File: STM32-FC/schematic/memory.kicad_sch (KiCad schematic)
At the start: 9 parts, among them J4 DM3AT-SF-PEJM5, U10 W25Q32JVUUIQ

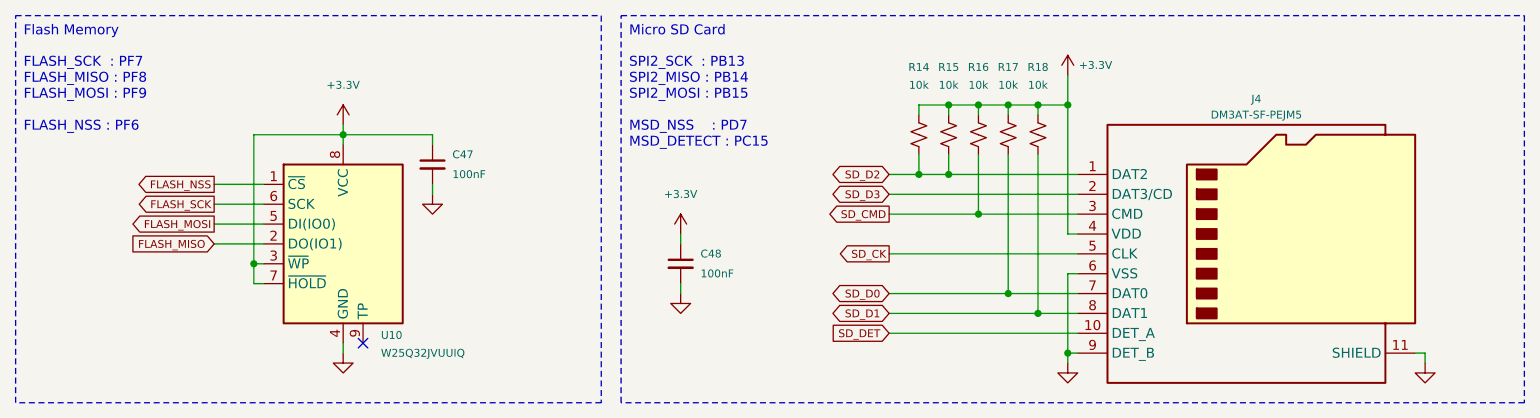
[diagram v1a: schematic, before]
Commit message: update : BOM and minor fix
- remove : DC2DC for analog
- change : JST SM conn. to BM
- change : ELRS conn. to JST XH (instead of JST SM)
- update : BOM List
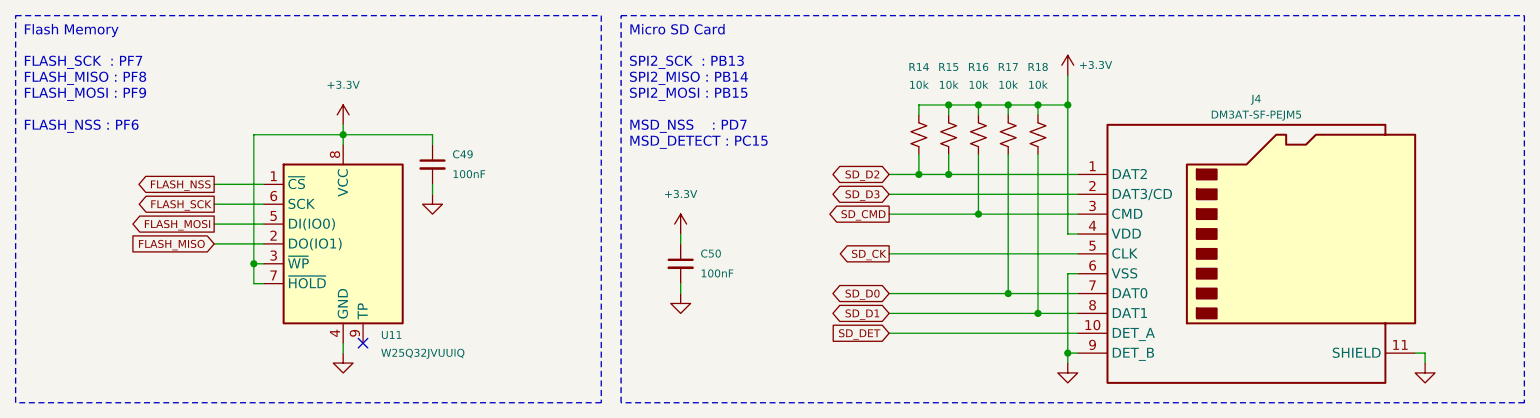
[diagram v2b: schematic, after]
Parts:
- renumbered C47 to C49, C48 to C50, U10 to U11
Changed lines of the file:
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@@
 		(dnp no)
 		(fields_autoplaced yes)
-		(property "Reference" "#PWR084"
+		(property "Reference" "#PWR089"
 			(at 107.95 54.61 0)
 			(effects
@@
 			(project ""
 				(path "/8d4cc317-3933-4aa6-844b-8c5c635e89c7/3e7c6c79-bc31-4cc9-af6a-d0a28245a7b2"
-					(reference "#PWR084")
+					(reference "#PWR089")
 					(unit 1)
 				)
@@
 		(dnp no)
 		(fields_autoplaced yes)
-		(property "Reference" "#PWR082"
+		(property "Reference" "#PWR087"
 			(at 76.2 41.91 0)
 			(effects
@@
 			(project ""
 				(path "/8d4cc317-3933-4aa6-844b-8c5c635e89c7/3e7c6c79-bc31-4cc9-af6a-d0a28245a7b2"
-					(reference "#PWR082")
+					(reference "#PWR087")
 					(unit 1)
 				)
@@
 		(dnp no)
 		(fields_autoplaced yes)
-		(property "Reference" "#PWR080"
+		(property "Reference" "#PWR085"
 			(at 64.77 30.48 0)
 			(effects
@@
 			(project ""
 				(path "/8d4cc317-3933-4aa6-844b-8c5c635e89c7/3e7c6c79-bc31-4cc9-af6a-d0a28245a7b2"
-					(reference "#PWR080")
+					(reference "#PWR085")
 					(unit 1)
 				)
@@
 		(dnp no)
 		(fields_autoplaced yes)
-		(property "Reference" "#PWR086"
+		(property "Reference" "#PWR091"
 			(at 157.48 63.5 0)
 			(effects
@@
 			(project "STM32-FC"
 				(path "/8d4cc317-3933-4aa6-844b-8c5c635e89c7/3e7c6c79-bc31-4cc9-af6a-d0a28245a7b2"
-					(reference "#PWR086")
+					(reference "#PWR091")
 					(unit 1)
 				)
@@
 		(on_board yes)
 		(dnp no)
-		(property "Reference" "C47"
+		(property "Reference" "C49"
 			(at 78.74 30.48 0)
 			(effects
@@
 			(project "STM32-FC"
 				(path "/8d4cc317-3933-4aa6-844b-8c5c635e89c7/3e7c6c79-bc31-4cc9-af6a-d0a28245a7b2"
-					(reference "C47")
+					(reference "C49")
 					(unit 1)
 				)
@@
 		(on_board yes)
 		(dnp no)
-		(property "Reference" "C48"
+		(property "Reference" "C50"
 			(at 110.49 43.18 0)
 			(effects
@@
 			(project "STM32-FC"
 				(path "/8d4cc317-3933-4aa6-844b-8c5c635e89c7/3e7c6c79-bc31-4cc9-af6a-d0a28245a7b2"
-					(reference "C48")
+					(reference "C50")
 					(unit 1)
 				)
@@
 		(dnp no)
 		(fields_autoplaced yes)
-		(property "Reference" "#PWR083"
+		(property "Reference" "#PWR088"
 			(at 107.95 44.45 0)
 			(effects
@@
 			(project ""
 				(path "/8d4cc317-3933-4aa6-844b-8c5c635e89c7/3e7c6c79-bc31-4cc9-af6a-d0a28245a7b2"
-					(reference "#PWR083")
+					(reference "#PWR088")
 					(unit 1)
 				)
@@
 		(dnp no)
 		(fields_autoplaced yes)
-		(property "Reference" "#PWR087"
+		(property "Reference" "#PWR092"
 			(at 203.2 63.5 0)
 			(effects
@@
 			(project "STM32-FC"
 				(path "/8d4cc317-3933-4aa6-844b-8c5c635e89c7/3e7c6c79-bc31-4cc9-af6a-d0a28245a7b2"
-					(reference "#PWR087")
+					(reference "#PWR092")
 					(unit 1)
 				)
@@
 		(dnp no)
 		(fields_autoplaced yes)
-		(property "Reference" "#PWR081"
+		(property "Reference" "#PWR086"
 			(at 64.77 62.23 0)
 			(effects
@@
 			(project ""
 				(path "/8d4cc317-3933-4aa6-844b-8c5c635e89c7/3e7c6c79-bc31-4cc9-af6a-d0a28245a7b2"
-					(reference "#PWR081")
+					(reference "#PWR086")
 					(unit 1)
 				)
@@
 		(on_board yes)
 		(dnp no)
-		(property "Reference" "U10"
+		(property "Reference" "U11"
 			(at 69.596 53.594 0)
 			(effects
@@
 			(project "STM32-FC"
 				(path "/8d4cc317-3933-4aa6-844b-8c5c635e89c7/3e7c6c79-bc31-4cc9-af6a-d0a28245a7b2"
-					(reference "U10")
+					(reference "U11")
 					(unit 1)
 				)
@@
 		(on_board yes)
 		(dnp no)
-		(property "Reference" "#PWR085"
+		(property "Reference" "#PWR090"
 			(at 157.48 24.13 0)
 			(effects
@@
 			(project "STM32-FC"
 				(path "/8d4cc317-3933-4aa6-844b-8c5c635e89c7/3e7c6c79-bc31-4cc9-af6a-d0a28245a7b2"
-					(reference "#PWR085")
+					(reference "#PWR090")
 					(unit 1)
 				)

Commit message: change : RC size 0402 to 0201
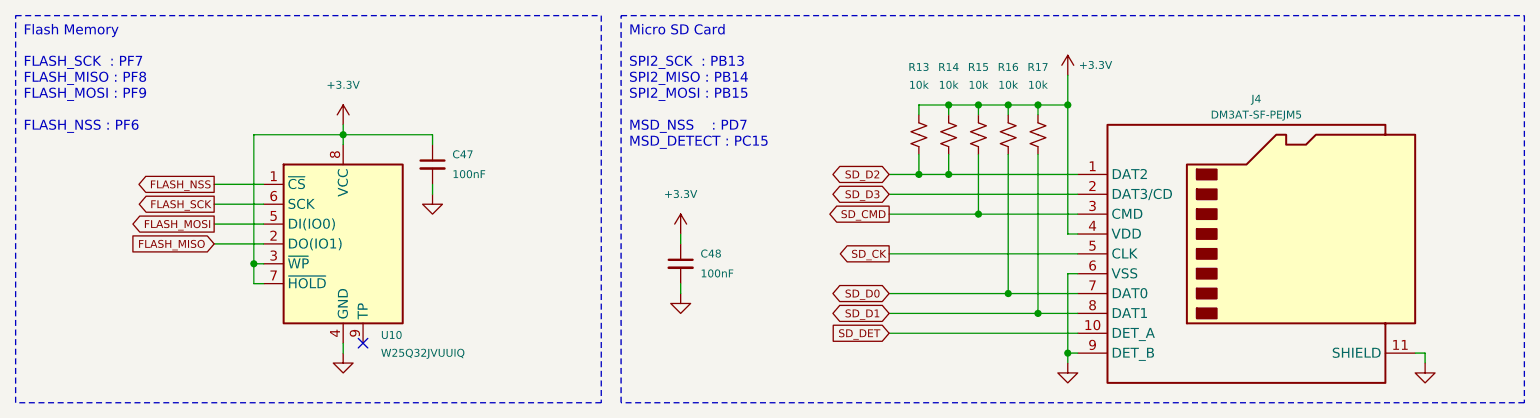
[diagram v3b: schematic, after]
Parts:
- C47: renamed from C49; footprint Capacitor_SMD:C_0402_1005Metric -> Capacitor_SMD:C_0201_0603Metric; LCSC C1525 -> C49062
- C48: renamed from C50; footprint Capacitor_SMD:C_0402_1005Metric -> Capacitor_SMD:C_0201_0603Metric; LCSC C1525 -> C49062
- R13: renamed from R14; footprint Resistor_SMD:R_0402_1005Metric -> Resistor_SMD:R_0201_0603Metric; LCSC C25531 -> C106225
- R14: renamed from R15; footprint Resistor_SMD:R_0402_1005Metric -> Resistor_SMD:R_0201_0603Metric; LCSC C25531 -> C106225
- R15: renamed from R16; footprint Resistor_SMD:R_0402_1005Metric -> Resistor_SMD:R_0201_0603Metric; LCSC C25531 -> C106225
- R16: renamed from R17; footprint Resistor_SMD:R_0402_1005Metric -> Resistor_SMD:R_0201_0603Metric; LCSC C25531 -> C106225
- R17: renamed from R18; footprint Resistor_SMD:R_0402_1005Metric -> Resistor_SMD:R_0201_0603Metric; LCSC C25531 -> C106225
- renumbered U11 to U10
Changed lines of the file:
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@@
 		(on_board yes)
 		(dnp no)
-		(property "Reference" "R18"
+		(property "Reference" "R17"
 			(at 153.67 19.304 0)
 			(effects
@@
 			)
 		)
-		(property "Footprint" "Resistor_SMD:R_0402_1005Metric"
+		(property "Footprint" "Resistor_SMD:R_0201_0603Metric"
 			(at 153.67 27.94 0)
 			(effects
@@
 			)
 		)
-		(property "Description" "Resistor, small US symbol"
+		(property "Description" "-55℃~+125℃ 10kΩ 25V 50mW Thick Film Resistor ±1% ±200ppm/℃ 0201 Chip Resistor - Surface Mount ROHS"
 			(at 153.67 27.94 0)
 			(effects
@@
 			)
 		)
-		(property "LCSC" "C25531"
+		(property "LCSC" "C106225"
 			(at 153.67 27.94 0)
 			(effects
@@
 			(project "STM32-FC"
 				(path "/8d4cc317-3933-4aa6-844b-8c5c635e89c7/3e7c6c79-bc31-4cc9-af6a-d0a28245a7b2"
-					(reference "R18")
+					(reference "R17")
 					(unit 1)
 				)
@@
 		(on_board yes)
 		(dnp no)
-		(property "Reference" "R17"
+		(property "Reference" "R16"
 			(at 149.86 19.304 0)
 			(effects
@@
 			)
 		)
-		(property "Footprint" "Resistor_SMD:R_0402_1005Metric"
+		(property "Footprint" "Resistor_SMD:R_0201_0603Metric"
 			(at 149.86 27.94 0)
 			(effects
@@
 			)
 		)
-		(property "Description" "Resistor, small US symbol"
+		(property "Description" "-55℃~+125℃ 10kΩ 25V 50mW Thick Film Resistor ±1% ±200ppm/℃ 0201 Chip Resistor - Surface Mount ROHS"
 			(at 149.86 27.94 0)
 			(effects
@@
 			)
 		)
-		(property "LCSC" "C25531"
+		(property "LCSC" "C106225"
 			(at 149.86 27.94 0)
 			(effects
@@
 			(project "STM32-FC"
 				(path "/8d4cc317-3933-4aa6-844b-8c5c635e89c7/3e7c6c79-bc31-4cc9-af6a-d0a28245a7b2"
-					(reference "R17")
+					(reference "R16")
 					(unit 1)
 				)
@@
 		(on_board yes)
 		(dnp no)
-		(property "Reference" "R16"
+		(property "Reference" "R15"
 			(at 146.05 19.304 0)
 			(effects
@@
 			)
 		)
-		(property "Footprint" "Resistor_SMD:R_0402_1005Metric"
+		(property "Footprint" "Resistor_SMD:R_0201_0603Metric"
 			(at 146.05 27.94 0)
 			(effects
@@
 			)
 		)
-		(property "Description" "Resistor, small US symbol"
+		(property "Description" "-55℃~+125℃ 10kΩ 25V 50mW Thick Film Resistor ±1% ±200ppm/℃ 0201 Chip Resistor - Surface Mount ROHS"
 			(at 146.05 27.94 0)
 			(effects
@@
 			)
 		)
-		(property "LCSC" "C25531"
+		(property "LCSC" "C106225"
 			(at 146.05 27.94 0)
 			(effects
@@
 			(project "STM32-FC"
 				(path "/8d4cc317-3933-4aa6-844b-8c5c635e89c7/3e7c6c79-bc31-4cc9-af6a-d0a28245a7b2"
-					(reference "R16")
+					(reference "R15")
 					(unit 1)
 				)
@@
 		(dnp no)
 		(fields_autoplaced yes)
-		(property "Reference" "#PWR089"
+		(property "Reference" "#PWR086"
 			(at 107.95 54.61 0)
 			(effects
@@
 			(project ""
 				(path "/8d4cc317-3933-4aa6-844b-8c5c635e89c7/3e7c6c79-bc31-4cc9-af6a-d0a28245a7b2"
-					(reference "#PWR089")
+					(reference "#PWR086")
 					(unit 1)
 				)
@@
 		(dnp no)
 		(fields_autoplaced yes)
-		(property "Reference" "#PWR087"
+		(property "Reference" "#PWR084"
 			(at 76.2 41.91 0)
 			(effects
@@
 			(project ""
 				(path "/8d4cc317-3933-4aa6-844b-8c5c635e89c7/3e7c6c79-bc31-4cc9-af6a-d0a28245a7b2"
-					(reference "#PWR087")
+					(reference "#PWR084")
 					(unit 1)
 				)
@@
 		(on_board yes)
 		(dnp no)
-		(property "Reference" "R14"
+		(property "Reference" "R13"
 			(at 138.43 19.304 0)
 			(effects
@@
 			)
 		)
-		(property "Footprint" "Resistor_SMD:R_0402_1005Metric"
+		(property "Footprint" "Resistor_SMD:R_0201_0603Metric"
 			(at 138.43 27.94 0)
 			(effects
@@
 			)
 		)
-		(property "Description" "Resistor, small US symbol"
+		(property "Description" "-55℃~+125℃ 10kΩ 25V 50mW Thick Film Resistor ±1% ±200ppm/℃ 0201 Chip Resistor - Surface Mount ROHS"
 			(at 138.43 27.94 0)
 			(effects
@@
 			)
 		)
-		(property "LCSC" "C25531"
+		(property "LCSC" "C106225"
 			(at 138.43 27.94 0)
 			(effects
@@
 			(project "STM32-FC"
 				(path "/8d4cc317-3933-4aa6-844b-8c5c635e89c7/3e7c6c79-bc31-4cc9-af6a-d0a28245a7b2"
-					(reference "R14")
+					(reference "R13")
 					(unit 1)
 				)
@@
 		(dnp no)
 		(fields_autoplaced yes)
-		(property "Reference" "#PWR085"
+		(property "Reference" "#PWR082"
 			(at 64.77 30.48 0)
 			(effects
@@
 			(project ""
 				(path "/8d4cc317-3933-4aa6-844b-8c5c635e89c7/3e7c6c79-bc31-4cc9-af6a-d0a28245a7b2"
-					(reference "#PWR085")
+					(reference "#PWR082")
 					(unit 1)
 				)
@@
 		(on_board yes)
 		(dnp no)
-		(property "Reference" "R15"
+		(property "Reference" "R14"
 			(at 142.24 19.304 0)
 			(effects
@@
 			)
 		)
-		(property "Footprint" "Resistor_SMD:R_0402_1005Metric"
+		(property "Footprint" "Resistor_SMD:R_0201_0603Metric"
 			(at 142.24 27.94 0)
 			(effects
@@
 			)
 		)
-		(property "Description" "Resistor, small US symbol"
+		(property "Description" "-55℃~+125℃ 10kΩ 25V 50mW Thick Film Resistor ±1% ±200ppm/℃ 0201 Chip Resistor - Surface Mount ROHS"
 			(at 142.24 27.94 0)
 			(effects
@@
 			)
 		)
-		(property "LCSC" "C25531"
+		(property "LCSC" "C106225"
 			(at 142.24 27.94 0)
 			(effects
@@
 			(project "STM32-FC"
 				(path "/8d4cc317-3933-4aa6-844b-8c5c635e89c7/3e7c6c79-bc31-4cc9-af6a-d0a28245a7b2"
-					(reference "R15")
+					(reference "R14")
 					(unit 1)
 				)
@@
 		(dnp no)
 		(fields_autoplaced yes)
-		(property "Reference" "#PWR091"
+		(property "Reference" "#PWR088"
 			(at 157.48 63.5 0)
 			(effects
@@
 			(project "STM32-FC"
 				(path "/8d4cc317-3933-4aa6-844b-8c5c635e89c7/3e7c6c79-bc31-4cc9-af6a-d0a28245a7b2"
-					(reference "#PWR091")
+					(reference "#PWR088")
 					(unit 1)
 				)
@@
 		(on_board yes)
 		(dnp no)
-		(property "Reference" "C49"
+		(property "Reference" "C47"
 			(at 78.74 30.48 0)
 			(effects
@@
 			)
 		)
-		(property "Footprint" "Capacitor_SMD:C_0402_1005Metric"
+		(property "Footprint" "Capacitor_SMD:C_0201_0603Metric"
 			(at 76.2 31.75 0)
 			(effects
@@
 			)
 		)
-		(property "Description" "Unpolarized capacitor, small symbol"
+		(property "Description" "100nF 10V X5R ±10% 0201 Multilayer Ceramic Capacitors MLCC - SMD/SMT ROHS"
 			(at 76.2 31.75 0)
 			(effects
@@
 			)
 		)
-		(property "LCSC" "C1525"
+		(property "LCSC" "C49062"
 			(at 76.2 31.75 0)
 			(effects
@@
 			(project "STM32-FC"
 				(path "/8d4cc317-3933-4aa6-844b-8c5c635e89c7/3e7c6c79-bc31-4cc9-af6a-d0a28245a7b2"
-					(reference "C49")
+					(reference "C47")
 					(unit 1)
 				)
@@
 		(on_board yes)
 		(dnp no)
-		(property "Reference" "C50"
+		(property "Reference" "C48"
 			(at 110.49 43.18 0)
 			(effects
@@
 			)
 		)
-		(property "Footprint" "Capacitor_SMD:C_0402_1005Metric"
+		(property "Footprint" "Capacitor_SMD:C_0201_0603Metric"
 			(at 107.95 44.45 0)
 			(effects
@@
 			)
 		)
-		(property "Description" "Unpolarized capacitor, small symbol"
+		(property "Description" "100nF 10V X5R ±10% 0201 Multilayer Ceramic Capacitors MLCC - SMD/SMT ROHS"
 			(at 107.95 44.45 0)
 			(effects
@@
 			)
 		)
-		(property "LCSC" "C1525"
+		(property "LCSC" "C49062"
 			(at 107.95 44.45 0)
 			(effects
@@
 			(project "STM32-FC"
 				(path "/8d4cc317-3933-4aa6-844b-8c5c635e89c7/3e7c6c79-bc31-4cc9-af6a-d0a28245a7b2"
-					(reference "C50")
+					(reference "C48")
 					(unit 1)
 				)
@@
 		(dnp no)
 		(fields_autoplaced yes)
-		(property "Reference" "#PWR088"
+		(property "Reference" "#PWR085"
 			(at 107.95 44.45 0)
 			(effects
@@
 			(project ""
 				(path "/8d4cc317-3933-4aa6-844b-8c5c635e89c7/3e7c6c79-bc31-4cc9-af6a-d0a28245a7b2"
-					(reference "#PWR088")
+					(reference "#PWR085")
 					(unit 1)
 				)
@@
 		(dnp no)
 		(fields_autoplaced yes)
-		(property "Reference" "#PWR092"
+		(property "Reference" "#PWR089"
 			(at 203.2 63.5 0)
 			(effects
@@
 			(project "STM32-FC"
 				(path "/8d4cc317-3933-4aa6-844b-8c5c635e89c7/3e7c6c79-bc31-4cc9-af6a-d0a28245a7b2"
-					(reference "#PWR092")
+					(reference "#PWR089")
 					(unit 1)
 				)
@@
 		(dnp no)
 		(fields_autoplaced yes)
-		(property "Reference" "#PWR086"
+		(property "Reference" "#PWR083"
 			(at 64.77 62.23 0)
 			(effects
@@
 			(project ""
 				(path "/8d4cc317-3933-4aa6-844b-8c5c635e89c7/3e7c6c79-bc31-4cc9-af6a-d0a28245a7b2"
-					(reference "#PWR086")
+					(reference "#PWR083")
 					(unit 1)
 				)
@@
 		(on_board yes)
 		(dnp no)
-		(property "Reference" "U11"
+		(property "Reference" "U10"
 			(at 69.596 53.594 0)
 			(effects
@@
 			(project "STM32-FC"
 				(path "/8d4cc317-3933-4aa6-844b-8c5c635e89c7/3e7c6c79-bc31-4cc9-af6a-d0a28245a7b2"
-					(reference "U11")
+					(reference "U10")
 					(unit 1)
 				)
@@
 		(on_board yes)
 		(dnp no)
-		(property "Reference" "#PWR090"
+		(property "Reference" "#PWR087"
 			(at 157.48 24.13 0)
 			(effects
@@
 			(project "STM32-FC"
 				(path "/8d4cc317-3933-4aa6-844b-8c5c635e89c7/3e7c6c79-bc31-4cc9-af6a-d0a28245a7b2"
-					(reference "#PWR090")
+					(reference "#PWR087")
 					(unit 1)
 				)
